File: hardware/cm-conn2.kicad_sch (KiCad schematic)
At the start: 1 part

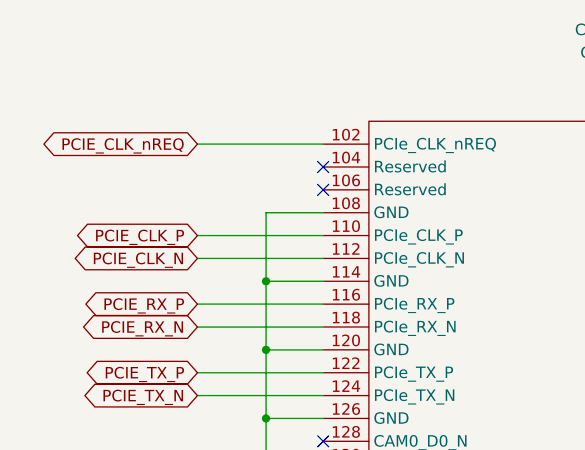
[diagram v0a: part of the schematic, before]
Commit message: Clean up ERC: PWR_FLAGs, OTG_ID solder jumper, PCIe_CLK_nREQ
- Add PWR_FLAG on GND net (PSU sheet)
- USB_OTG_ID: solder jumper to GND with 10K pull-up for host/device mode
- PCIe_CLK_nREQ tied to GND locally on connector 2
- 1 ERC error remaining: CM4 dual 3.3V output pins (false positive)
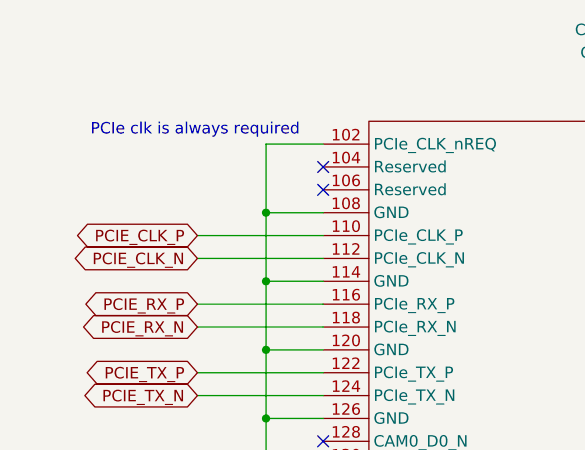
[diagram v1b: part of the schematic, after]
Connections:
- net PCIE_CLK_nREQ is gone; now on net GND: CM1.102 (PCIe_CLK_nREQ)
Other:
- note added: "PCIe clk is always required"
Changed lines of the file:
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@@
 		(comment 2 "Git commit hash: ${GIT_HASH}")
 	)
+	(text "PCIe clk is always required\n"
+		(exclude_from_sim no)
+		(at 44.196 41.656 0)
+		(effects
+			(font
+				(size 1.27 1.27)
+			)
+		)
+	)
 	(junction
 		(at 52.07 149.86)
@@
 	)
 	(junction
+		(at 52.07 50.8)
+		(diameter 0)
+		(color 0 0 0 0)
+	)
+	(junction
 		(at 52.07 157.48)
 		(diameter 0)
@@
 	(wire
 		(pts
-			(xy 44.45 43.18) (xy 58.42 43.18)
+			(xy 52.07 43.18) (xy 58.42 43.18)
 		)
 		(stroke
@@
 		(pts
 			(xy 133.35 142.24) (xy 133.35 149.86)
+		)
+		(stroke
+			(width 0)
+			(type default)
+		)
+	)
+	(wire
+		(pts
+			(xy 52.07 43.18) (xy 52.07 50.8)
 		)
 		(stroke
@@
 			(hide yes)
 			(show_name no)
-			(do_not_autoplace no)
-			(effects
-				(font
-					(size 1.27 1.27)
-				)
-				(justify right)
-			)
-		)
-	)
-	(global_label "PCIE_CLK_nREQ"
-		(shape bidirectional)
-		(at 44.45 43.18 180)
-		(fields_autoplaced yes)
-		(effects
-			(font
-				(size 1.27 1.27)
-			)
-			(justify right)
-		)
-		(property "Intersheetrefs" "${INTERSHEET_REFS}"
-			(at 25.6579 43.18 0)
-			(hide yes)
-			(show_name no)
